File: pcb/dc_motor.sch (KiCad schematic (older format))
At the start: 62 parts, among them J1 Conn_01x02, J2 Conn_01x04, J3 Conn_01x04, J4 Conn_01x07, Q1 IPD90P03P4L04, Q2 BTN8982TA, Q3 BTN8982TA, U1 L7805, U2 INA226, U3 74AHC244

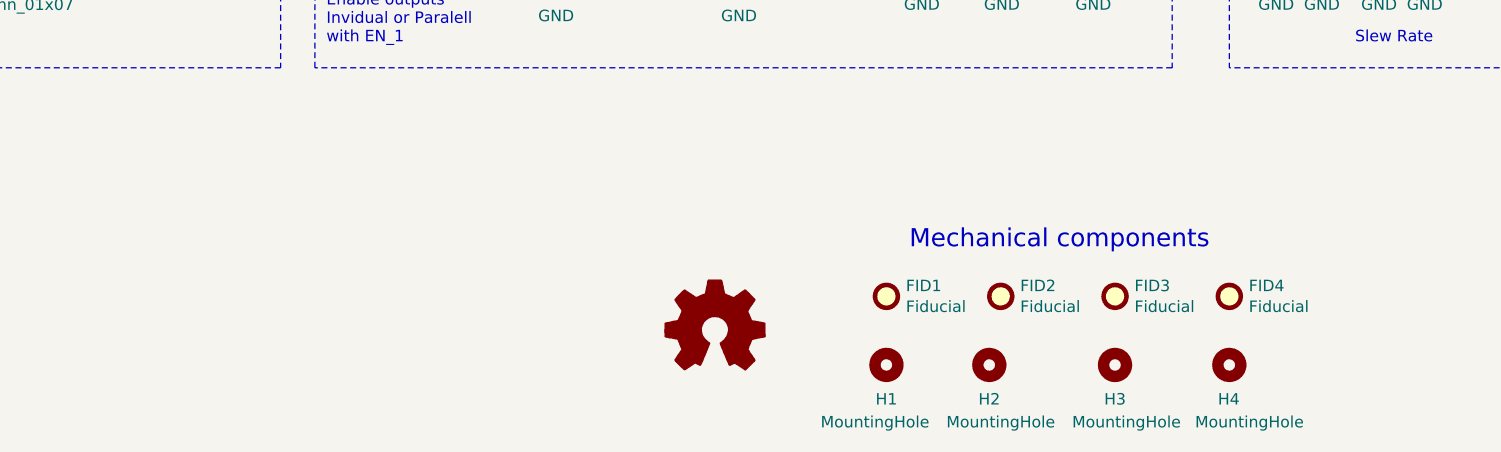
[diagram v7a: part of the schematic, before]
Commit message: add open hardware logo
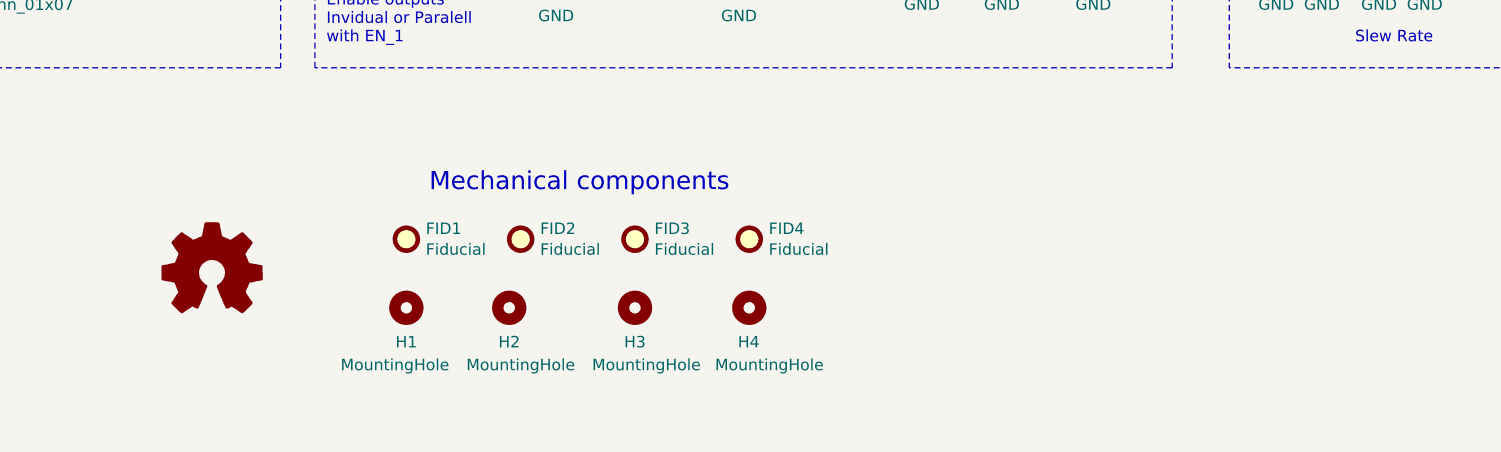
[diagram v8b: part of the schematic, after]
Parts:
- added LOGO1: Logo_Open_Hardware_Small, Symbol:OSHW-Logo2_9.8x8mm_SilkScreen, symbol Graphic:Logo_Open_Hardware_Small
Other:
- moved on the sheet: FID1, FID2, FID3, FID4, H1, H2, H3, H4
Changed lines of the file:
@@
 Sheet 1 1
 Title "DC MOTOR CONTROL"
-Date "2020-09-11"
+Date "2020-11-04"
 Rev "1.0"
 Comp "NOVOTEC ARGENTINA SRL"
@@
 L Mechanical:MountingHole H1
 U 1 1 5F66DB68
-P 5000 7300
-F 0 "H1" H 5000 7150 50  0000 C CNN
-F 1 "MountingHole" H 4950 7050 50  0000 C CNN
-F 2 "MountingHole:MountingHole_3.2mm_M3_ISO14580" H 5000 7300 50  0001 C CNN
-F 3 "~" H 5000 7300 50  0001 C CNN
-F 4 "NF" H 5000 7300 50  0001 C CNN "Manufacturer Part Number"
-F 5 "NF" H 5000 7300 50  0001 C CNN "Supplier 1 Part Number"
-	1    5000 7300
+P 2900 7050
+F 0 "H1" H 2900 6900 50  0000 C CNN
+F 1 "MountingHole" H 2850 6800 50  0000 C CNN
+F 2 "MountingHole:MountingHole_3.2mm_M3_ISO14580" H 2900 7050 50  0001 C CNN
+F 3 "~" H 2900 7050 50  0001 C CNN
+F 4 "NF" H 2900 7050 50  0001 C CNN "Manufacturer Part Number"
+F 5 "NF" H 2900 7050 50  0001 C CNN "Supplier 1 Part Number"
+	1    2900 7050
 	1    0    0    -1
 $EndComp
@@
 L Mechanical:MountingHole H2
 U 1 1 5F674F12
-P 5450 7300
-F 0 "H2" H 5450 7150 50  0000 C CNN
-F 1 "MountingHole" H 5500 7050 50  0000 C CNN
-F 2 "MountingHole:MountingHole_3.2mm_M3_ISO14580" H 5450 7300 50  0001 C CNN
-F 3 "~" H 5450 7300 50  0001 C CNN
-F 4 "NF" H 5450 7300 50  0001 C CNN "Manufacturer Part Number"
-F 5 "NF" H 5450 7300 50  0001 C CNN "Supplier 1 Part Number"
-	1    5450 7300
+P 3350 7050
+F 0 "H2" H 3350 6900 50  0000 C CNN
+F 1 "MountingHole" H 3400 6800 50  0000 C CNN
+F 2 "MountingHole:MountingHole_3.2mm_M3_ISO14580" H 3350 7050 50  0001 C CNN
+F 3 "~" H 3350 7050 50  0001 C CNN
+F 4 "NF" H 3350 7050 50  0001 C CNN "Manufacturer Part Number"
+F 5 "NF" H 3350 7050 50  0001 C CNN "Supplier 1 Part Number"
+	1    3350 7050
 	1    0    0    -1
 $EndComp
@@
 L Mechanical:MountingHole H3
 U 1 1 5F679C7D
-P 6000 7300
-F 0 "H3" H 6000 7150 50  0000 C CNN
-F 1 "MountingHole" H 6050 7050 50  0000 C CNN
-F 2 "MountingHole:MountingHole_3.2mm_M3_ISO14580" H 6000 7300 50  0001 C CNN
-F 3 "~" H 6000 7300 50  0001 C CNN
-F 4 "NF" H 6000 7300 50  0001 C CNN "Manufacturer Part Number"
-F 5 "NF" H 6000 7300 50  0001 C CNN "Supplier 1 Part Number"
-	1    6000 7300
+P 3900 7050
+F 0 "H3" H 3900 6900 50  0000 C CNN
+F 1 "MountingHole" H 3950 6800 50  0000 C CNN
+F 2 "MountingHole:MountingHole_3.2mm_M3_ISO14580" H 3900 7050 50  0001 C CNN
+F 3 "~" H 3900 7050 50  0001 C CNN
+F 4 "NF" H 3900 7050 50  0001 C CNN "Manufacturer Part Number"
+F 5 "NF" H 3900 7050 50  0001 C CNN "Supplier 1 Part Number"
+	1    3900 7050
 	1    0    0    -1
 $EndComp
@@
 L Mechanical:MountingHole H4
 U 1 1 5F67EA56
-P 6500 7300
-F 0 "H4" H 6450 7150 50  0000 L CNN
-F 1 "MountingHole" H 6350 7050 50  0000 L CNN
-F 2 "MountingHole:MountingHole_3.2mm_M3_ISO14580" H 6500 7300 50  0001 C CNN
-F 3 "~" H 6500 7300 50  0001 C CNN
-F 4 "NF" H 6500 7300 50  0001 C CNN "Manufacturer Part Number"
-F 5 "NF" H 6500 7300 50  0001 C CNN "Supplier 1 Part Number"
-	1    6500 7300
+P 4400 7050
+F 0 "H4" H 4350 6900 50  0000 L CNN
+F 1 "MountingHole" H 4250 6800 50  0000 L CNN
+F 2 "MountingHole:MountingHole_3.2mm_M3_ISO14580" H 4400 7050 50  0001 C CNN
+F 3 "~" H 4400 7050 50  0001 C CNN
+F 4 "NF" H 4400 7050 50  0001 C CNN "Manufacturer Part Number"
+F 5 "NF" H 4400 7050 50  0001 C CNN "Supplier 1 Part Number"
+	1    4400 7050
 	1    0    0    -1
 $EndComp
@@
 L Mechanical:Fiducial FID1
 U 1 1 5F6CECAA
-P 5000 7000
-F 0 "FID1" H 5085 7046 50  0000 L CNN
-F 1 "Fiducial" H 5085 6955 50  0000 L CNN
-F 2 "Fiducial:Fiducial_0.5mm_Mask1.5mm" H 5000 7000 50  0001 C CNN
-F 3 "~" H 5000 7000 50  0001 C CNN
-F 4 "NF" H 5000 7000 50  0001 C CNN "Manufacturer Part Number"
-F 5 "NF" H 5000 7000 50  0001 C CNN "Supplier 1 Part Number"
-	1    5000 7000
+P 2900 6750
+F 0 "FID1" H 2985 6796 50  0000 L CNN
+F 1 "Fiducial" H 2985 6705 50  0000 L CNN
+F 2 "Fiducial:Fiducial_0.5mm_Mask1.5mm" H 2900 6750 50  0001 C CNN
+F 3 "~" H 2900 6750 50  0001 C CNN
+F 4 "NF" H 2900 6750 50  0001 C CNN "Manufacturer Part Number"
+F 5 "NF" H 2900 6750 50  0001 C CNN "Supplier 1 Part Number"
+	1    2900 6750
 	1    0    0    -1
 $EndComp
@@
 L Mechanical:Fiducial FID2
 U 1 1 5F6CF4FC
-P 5500 7000
-F 0 "FID2" H 5585 7046 50  0000 L CNN
-F 1 "Fiducial" H 5585 6955 50  0000 L CNN
-F 2 "Fiducial:Fiducial_0.5mm_Mask1.5mm" H 5500 7000 50  0001 C CNN
-F 3 "~" H 5500 7000 50  0001 C CNN
-F 4 "NF" H 5500 7000 50  0001 C CNN "Manufacturer Part Number"
-F 5 "NF" H 5500 7000 50  0001 C CNN "Supplier 1 Part Number"
-	1    5500 7000
+P 3400 6750
+F 0 "FID2" H 3485 6796 50  0000 L CNN
+F 1 "Fiducial" H 3485 6705 50  0000 L CNN
+F 2 "Fiducial:Fiducial_0.5mm_Mask1.5mm" H 3400 6750 50  0001 C CNN
+F 3 "~" H 3400 6750 50  0001 C CNN
+F 4 "NF" H 3400 6750 50  0001 C CNN "Manufacturer Part Number"
+F 5 "NF" H 3400 6750 50  0001 C CNN "Supplier 1 Part Number"
+	1    3400 6750
 	1    0    0    -1
 $EndComp
@@
 L Mechanical:Fiducial FID3
 U 1 1 5F6D41FF
-P 6000 7000
-F 0 "FID3" H 6085 7046 50  0000 L CNN
-F 1 "Fiducial" H 6085 6955 50  0000 L CNN
-F 2 "Fiducial:Fiducial_0.5mm_Mask1.5mm" H 6000 7000 50  0001 C CNN
-F 3 "~" H 6000 7000 50  0001 C CNN
-F 4 "NF" H 6000 7000 50  0001 C CNN "Manufacturer Part Number"
-F 5 "NF" H 6000 7000 50  0001 C CNN "Supplier 1 Part Number"
-	1    6000 7000
+P 3900 6750
+F 0 "FID3" H 3985 6796 50  0000 L CNN
+F 1 "Fiducial" H 3985 6705 50  0000 L CNN
+F 2 "Fiducial:Fiducial_0.5mm_Mask1.5mm" H 3900 6750 50  0001 C CNN
+F 3 "~" H 3900 6750 50  0001 C CNN
+F 4 "NF" H 3900 6750 50  0001 C CNN "Manufacturer Part Number"
+F 5 "NF" H 3900 6750 50  0001 C CNN "Supplier 1 Part Number"
+	1    3900 6750
 	1    0    0    -1
 $EndComp
@@
 L Mechanical:Fiducial FID4
 U 1 1 5F6D8F8C
-P 6500 7000
-F 0 "FID4" H 6585 7046 50  0000 L CNN
-F 1 "Fiducial" H 6585 6955 50  0000 L CNN
-F 2 "Fiducial:Fiducial_0.5mm_Mask1.5mm" H 6500 7000 50  0001 C CNN
-F 3 "~" H 6500 7000 50  0001 C CNN
-F 4 "NF" H 6500 7000 50  0001 C CNN "Manufacturer Part Number"
-F 5 "NF" H 6500 7000 50  0001 C CNN "Supplier 1 Part Number"
-	1    6500 7000
-	1    0    0    -1
-$EndComp
-Text Notes 5100 6800 0    79   ~ 0
+P 4400 6750
+F 0 "FID4" H 4485 6796 50  0000 L CNN
+F 1 "Fiducial" H 4485 6705 50  0000 L CNN
+F 2 "Fiducial:Fiducial_0.5mm_Mask1.5mm" H 4400 6750 50  0001 C CNN
+F 3 "~" H 4400 6750 50  0001 C CNN
+F 4 "NF" H 4400 6750 50  0001 C CNN "Manufacturer Part Number"
+F 5 "NF" H 4400 6750 50  0001 C CNN "Supplier 1 Part Number"
+	1    4400 6750
+	1    0    0    -1
+$EndComp
+Text Notes 3000 6550 0    79   ~ 0
 Mechanical components
 Wire Notes Line width 10
@@
 uC Interface
 $Comp
-L Graphic:Logo_Open_Hardware_Small #LOGO1
+L Graphic:Logo_Open_Hardware_Small LOGO1
 U 1 1 60307894
-P 4250 7150
-F 0 "#LOGO1" H 4250 7425 50  0001 C CNN
-F 1 "Logo_Open_Hardware_Small" H 4250 6925 50  0001 C CNN
-F 2 "" H 4250 7150 50  0001 C CNN
-F 3 "~" H 4250 7150 50  0001 C CNN
-	1    4250 7150
-	1    0    0    -1
-$EndComp
+P 2050 6900
+F 0 "LOGO1" H 2050 7175 50  0001 C CNN
+F 1 "Logo_Open_Hardware_Small" H 2050 6675 50  0001 C CNN
+F 2 "Symbol:OSHW-Logo2_9.8x8mm_SilkScreen" H 2050 6900 50  0001 C CNN
+F 3 "~" H 2050 6900 50  0001 C CNN
+	1    2050 6900
+	1    0    0    -1
+$EndComp
